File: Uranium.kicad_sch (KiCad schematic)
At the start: 48 parts, among them J1 Conn_ARM_JTAG_SWD_10, J2 USB_C_Receptacle_USB2.0, Q1 DTC123J, SW1 SW_Push, SW2 Rotary_Encoder_Switch, U1 74HCT245PW, U2 STM32F072CBUx, U3 USBLC6-2SC6, U4 MCP1700-3302E_SOT23

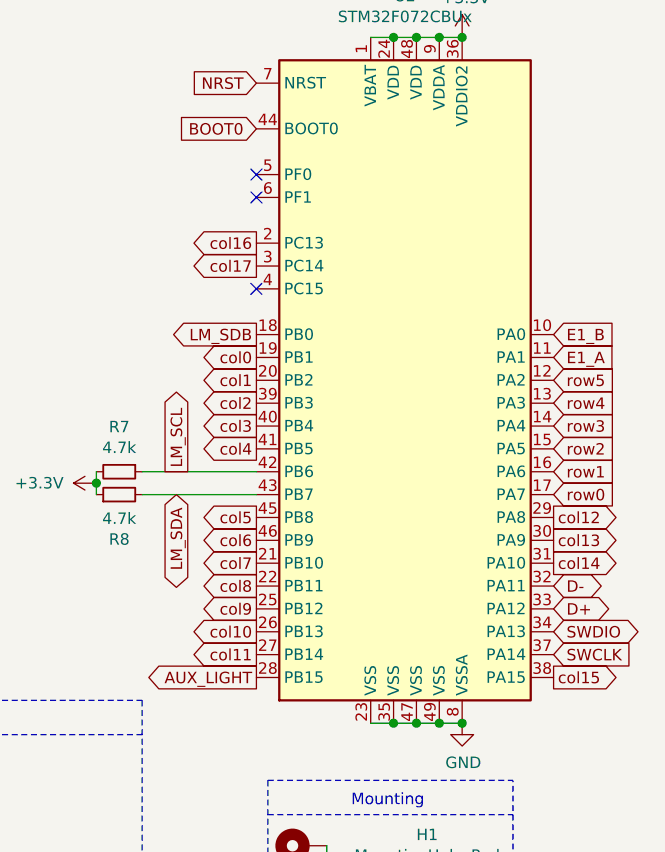
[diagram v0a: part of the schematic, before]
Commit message: Wired up keyboard so it is an MVP
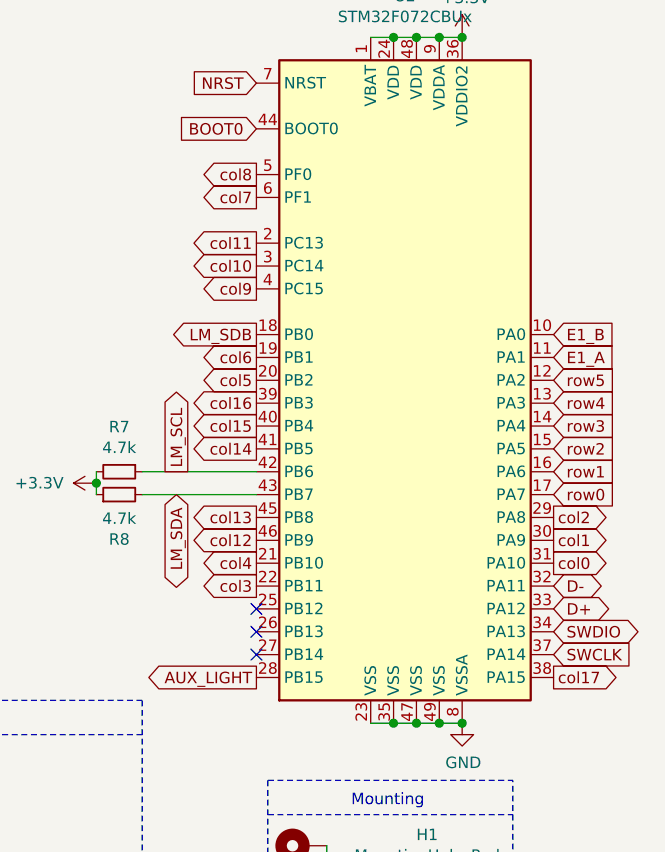
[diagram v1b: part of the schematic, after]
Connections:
- net col0: now also U2.31 (PA10); no longer U2.19 (PB1)
- net col1: now also U2.30 (PA9); no longer U2.20 (PB2)
- net col10: now also U2.3 (PC14); no longer U2.26 (PB13)
- net col11: now also U2.2 (PC13); no longer U2.27 (PB14)
- net col12: now also U2.46 (PB9); no longer U2.29 (PA8)
- net col13: now also U2.45 (PB8); no longer U2.30 (PA9)
- net col14: now also U2.41 (PB5); no longer U2.31 (PA10)
- net col15: now also U2.40 (PB4); no longer U2.38 (PA15)
- net col16: now also U2.39 (PB3); no longer U2.2 (PC13)
- net col17: now also U2.38 (PA15); no longer U2.3 (PC14)
- net col2: now also U2.29 (PA8); no longer U2.39 (PB3)
- net col3: now also U2.22 (PB11); no longer U2.40 (PB4)
- net col4: now also U2.21 (PB10); no longer U2.41 (PB5)
- net col5: now also U2.20 (PB2); no longer U2.45 (PB8)
- net col6: now also U2.19 (PB1); no longer U2.46 (PB9)
- net col7: now also U2.6 (PF1); no longer U2.21 (PB10)
- net col8: now also U2.5 (PF0); no longer U2.22 (PB11)
- net col9: now also U2.4 (PC15); no longer U2.25 (PB12)
